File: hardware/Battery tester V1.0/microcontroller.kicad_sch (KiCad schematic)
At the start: 17 parts, among them IC4 PIC18F67J50, J1 USB_B, J2 ICP

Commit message: update man pcb, cleanup
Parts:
- removed C?: 470u/10V, Capacitor_THT:CP_Radial_D8.0mm_P3.80mm, symbol Device:C_Polarized
- removed C?: 100n, Capacitor_SMD:C_0805_2012Metric_Pad1.18x1.45mm_HandSolder, symbol Device:C
- removed LCD1: RG12864B-BIW-V, symbol My-Lib:RG12864B-BIW-V
- removed Q?: BC817, Package_TO_SOT_SMD:SOT-23, symbol Transistor_BJT:BC817
- removed R? (x2): 10k, Resistor_SMD:R_0805_2012Metric, symbol Device:R
- removed R? (x2): R, Resistor_SMD:R_1206_3216Metric, symbol Device:R
- removed R? (x2): R, Resistor_SMD:R_0805_2012Metric_Pad1.20x1.40mm_HandSolder, symbol Device:R
- removed RV?: 10k, Potentiometer_THT:Potentiometer_ACP_CA9-V10_Vertical_Hole, symbol Device:R_Potentiometer
- added C10: 1u, Capacitor_SMD:C_0805_2012Metric_Pad1.18x1.45mm_HandSolder, symbol Device:C
- added C5, C6, C7, C9: 100n, Capacitor_SMD:C_0805_2012Metric_Pad1.18x1.45mm_HandSolder, symbol Device:C
- added C8: 10u, Capacitor_SMD:C_1206_3216Metric_Pad1.33x1.80mm_HandSolder, symbol Device:C
- added J3: VCC_5V, Connector_JST:JST_XA_B02B-XASK-1_1x02_P2.50mm_Vertical, symbol Connector_Generic:Conn_01x02
- added J3, J4: LED, Connector_IDC:IDC-Header_2x05_P2.54mm_Vertical, symbol Connector_Generic:Conn_02x05_Counter_Clockwise
- added R11: 510R, symbol Device:R
- added U2: TL431DBZ, Package_TO_SOT_SMD:SOT-23, symbol Reference_Voltage:TL431DBZ
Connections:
- net +3.3V: now also C5.1, C6.1, C7.1, R11.2
- net +5V: now also J3.2 (Pin_2)
- net CS1: now also J4.6 (Pin_6)
- net CS2: now also J4.8 (Pin_8)
- net DB0: now also J4.1 (Pin_1)
- net DB1: now also J4.2 (Pin_2)
- net DB2: now also J4.3 (Pin_3)
- net DB3: now also J4.4 (Pin_4)
- net DB4: now also J4.5 (Pin_5)
- net DB5: now also J4.7 (Pin_7)
- net DB6: now also J4.9 (Pin_9)
- net DB7: now also J4.10 (Pin_10)
- net DI: now also J3.2 (Pin_2)
- net EN: now also J3.3 (Pin_3)
- net GND: now also C10.2, C5.2, C6.2, C7.2, C8.2, C9.2, J3.1 (Pin_1), U2.3 (A)
- net LCD_BACKLIGHT: now also IC4.3 (RG0/PMA8/ECCP3/P3A), J3.4 (Pin_4); no longer IC4.50 (RD6/PMD6/SCK2/SCL2)
- net ~{RST}: now also J3.1 (Pin_1); no longer IC4.51 (RD5/PMD5/SDI2/SDA2)
- net at IC4.10 (VDDCORE/VCAP): now also C8.1
- net SWITCH_RANGE: now reaches IC4.13 (RF5/AN10/C1INB/CVREF)
- net VREF_2V5: now reaches IC4.21 (RA3/AN3/VREF+)
- net VREF_2V5: now also C10.1, C9.1, R11.1, U2.1 (K), U2.2 (REF)
- net RW: no longer names the net of IC4.52 (RD4/PMD4/SDO2)
- new net COL1: J3.5 (Pin_5)
- new net COL2: J3.6 (Pin_6)
- new net COL3: J3.7 (Pin_7)
- new net ROW1: J3.8 (Pin_8)
- new net ROW2: J3.9 (Pin_9)
- new net ROW3: J3.10 (Pin_10)
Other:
- note added: "2V5 VOLTAGE REFRENCE"
- note added: "LCD, PUSH BUTTONS CONNECTORS"
- note added: "PROGRAMMING INTERFACE"
- moved on the sheet: J2, R10

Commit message: update main pcb schematic
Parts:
- added C11, C13: 100n, Capacitor_SMD:C_0805_2012Metric_Pad1.18x1.45mm_HandSolder, symbol Device:C
- added C12: 1u, Capacitor_SMD:C_0805_2012Metric_Pad1.18x1.45mm_HandSolder, symbol Device:C
- added R13, R14: 56k, Capacitor_SMD:C_0805_2012Metric_Pad1.18x1.45mm_HandSolder, symbol Device:R
- added U3: MCP4725xxx-xCH, Package_TO_SOT_SMD:SOT-23-6, symbol Analog_DAC:MCP4725xxx-xCH
- added U4: SST25VF016B, Package_SO:SOIC-8_5.3x5.3mm_P1.27mm, symbol Memory_Flash:SST25VF080B-50-4x-S2Ax
- added U5: DS18B20, Package_TO_SOT_THT:TO-92_Inline, symbol Sensor_Temperature:DS18B20
- J1: footprint (none) -> Connector_USB:USB_B_Lumberg_2411_02_Horizontal
- J5: renamed from J2; footprint (none) -> Connector_PinSocket_2.54mm:PinSocket_1x06_P2.54mm_Vertical
- R1: renamed from R11; footprint (none) -> Capacitor_SMD:C_0805_2012Metric_Pad1.18x1.45mm_HandSolder
- R2: renamed from R1; footprint (none) -> Capacitor_SMD:C_0805_2012Metric_Pad1.18x1.45mm_HandSolder
- R3: renamed from R2; footprint (none) -> Capacitor_SMD:C_0805_2012Metric_Pad1.18x1.45mm_HandSolder
- R4: renamed from R10; footprint (none) -> Capacitor_SMD:C_0805_2012Metric_Pad1.18x1.45mm_HandSolder
- renumbered C8 to C1, C6 to C2, C5 to C3, C7 to C4, C10 to C5, C9 to C6, IC4 to IC1, J3 to J2, J4 to J3, J3 to J4, U2 to U1
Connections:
- net +3.3V: now also C11.1, C12.1, C13.1, R13.2, R14.2, U3.3 (VDD), U4.3 (~{WP}), U4.7 (~{HOLD}), U4.8 (VDD), U5.3 (V_{DD})
- net DBG_UART: now also IC1.31 (RC6/TX1/CK1)
- net GND: now also C11.2, C12.2, C13.2, U3.2 (VSS), U3.6 (A0), U4.4 (VSS), U5.1 (GND)
- net PGC: now also IC1.42 (RB6/KBI2/PGC)
- net PGD: now also IC1.37 (RB7/KBI3/PGD)
- net GNDA: now reaches IC1.20 (AVSS)
- net ADC_CHARGE_VOLTAGE: now reaches IC1.22 (RA2/AN2/VREF-)
- net ADC_CHARGE_CURRENT: now reaches IC1.23 (RA1/AN1)
- net SCL: now reaches IC1.34 (RC3/SCK1/SCL1)
- net SCL: now also R13.1, U3.5 (SCL)
- net SDA: now reaches IC1.35 (RC4/SDI1/SDA1)
- net SDA: now also R14.1, U3.4 (SDA)
- net DS18B20: now reaches IC1.48 (RB0/FLT0/INT0)
- net DS18B20: now also U5.2 (DQ)
- net FLASH_CS: now reaches IC1.49 (RD7/PMD7/~{SS2})
- net FLASH_CS: now also U4.1 (~{CE})
- net FLASH_SCK: now reaches IC1.50 (RD6/PMD6/SCK2/SCL2)
- net FLASH_SCK: now also U4.6 (SCK)
- net FLASH_SDI: now reaches IC1.51 (RD5/PMD5/SDI2/SDA2)
- net FLASH_SDI: now also U4.5 (SI)
- net FLASH_SDO: now reaches IC1.52 (RD4/PMD4/SDO2)
- net FLASH_SDO: now also U4.2 (SO)
- new net DAC_CURRENT: U3.1 (VOUT)
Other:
- note added: "12BIT I2C DAC FOR CURRENT REGULATION"
- note added: "16MBIT SPI FLASH MEMORY"

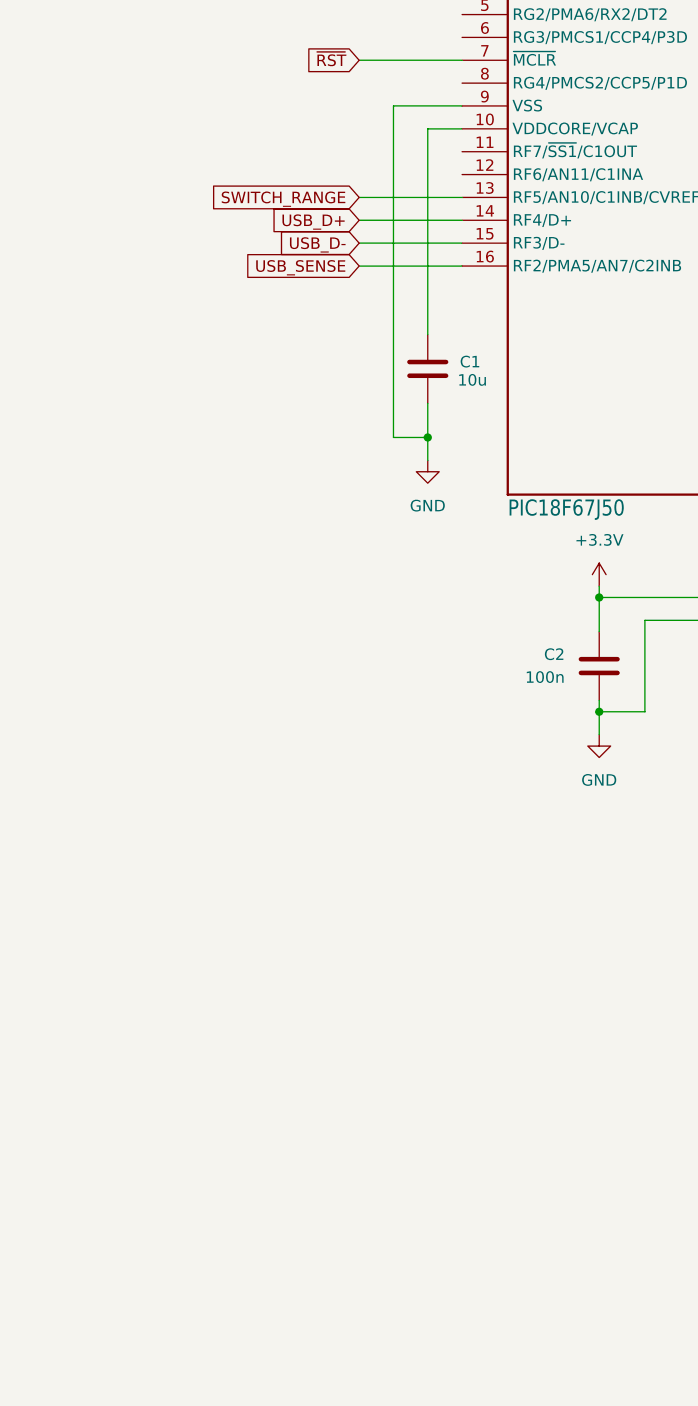
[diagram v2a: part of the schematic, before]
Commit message: update main pcb battery charger
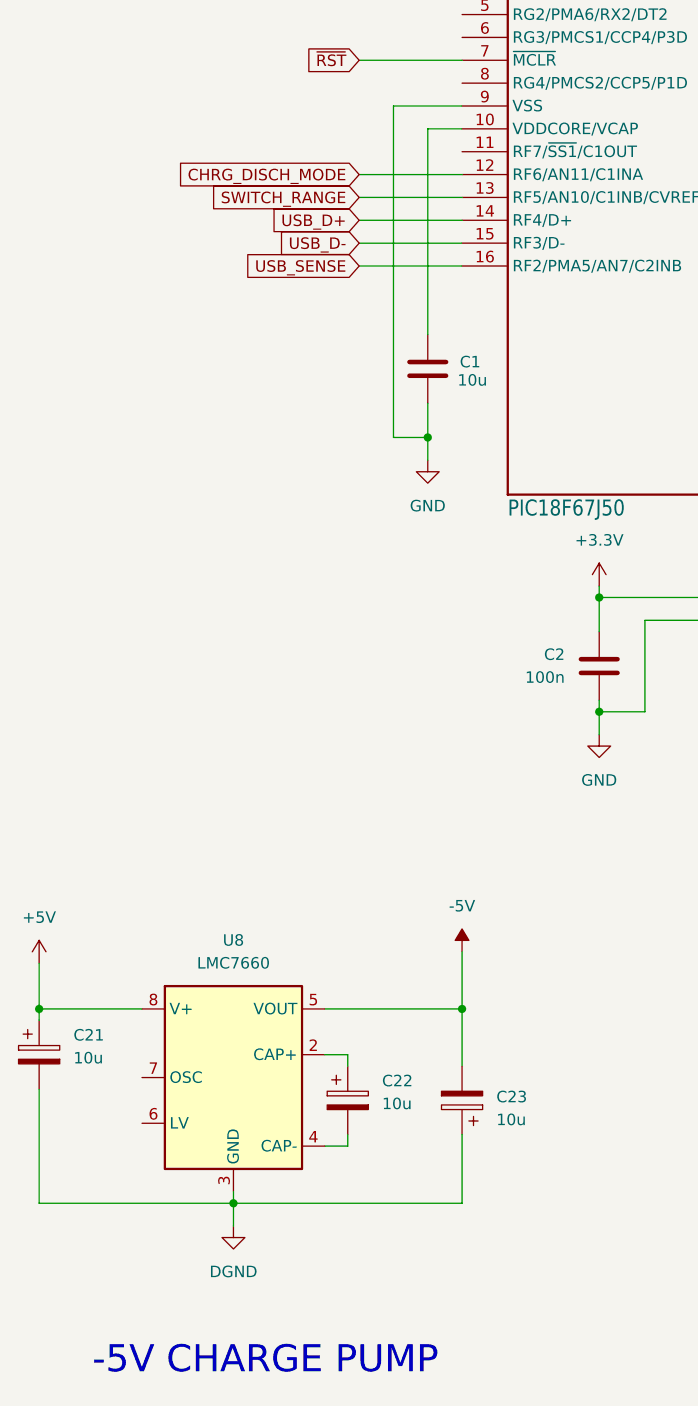
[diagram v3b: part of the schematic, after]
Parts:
- added C21, C22, C23: 10u, Capacitor_Tantalum_SMD:CP_EIA-3528-12_Kemet-T, symbol Device:C_Polarized
- added U8: LMC7660, Package_SO:SOIC-8_3.9x4.9mm_P1.27mm, symbol Regulator_SwitchedCapacitor:LMC7660
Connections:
- net +5V: now also C21.1, U8.8 (V+)
- net CHRG_DISCH_MODE: now reaches IC1.12 (RF6/AN11/C1INA)
- new net: C22.1, U8.2 (CAP+)
- new net: C22.2, U8.4 (CAP-)
- new net -5V: C23.2, U8.5 (VOUT)
- new net DGND: C21.2, C23.1, U8.3 (GND)
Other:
- note added: "-5V CHARGE PUMP"

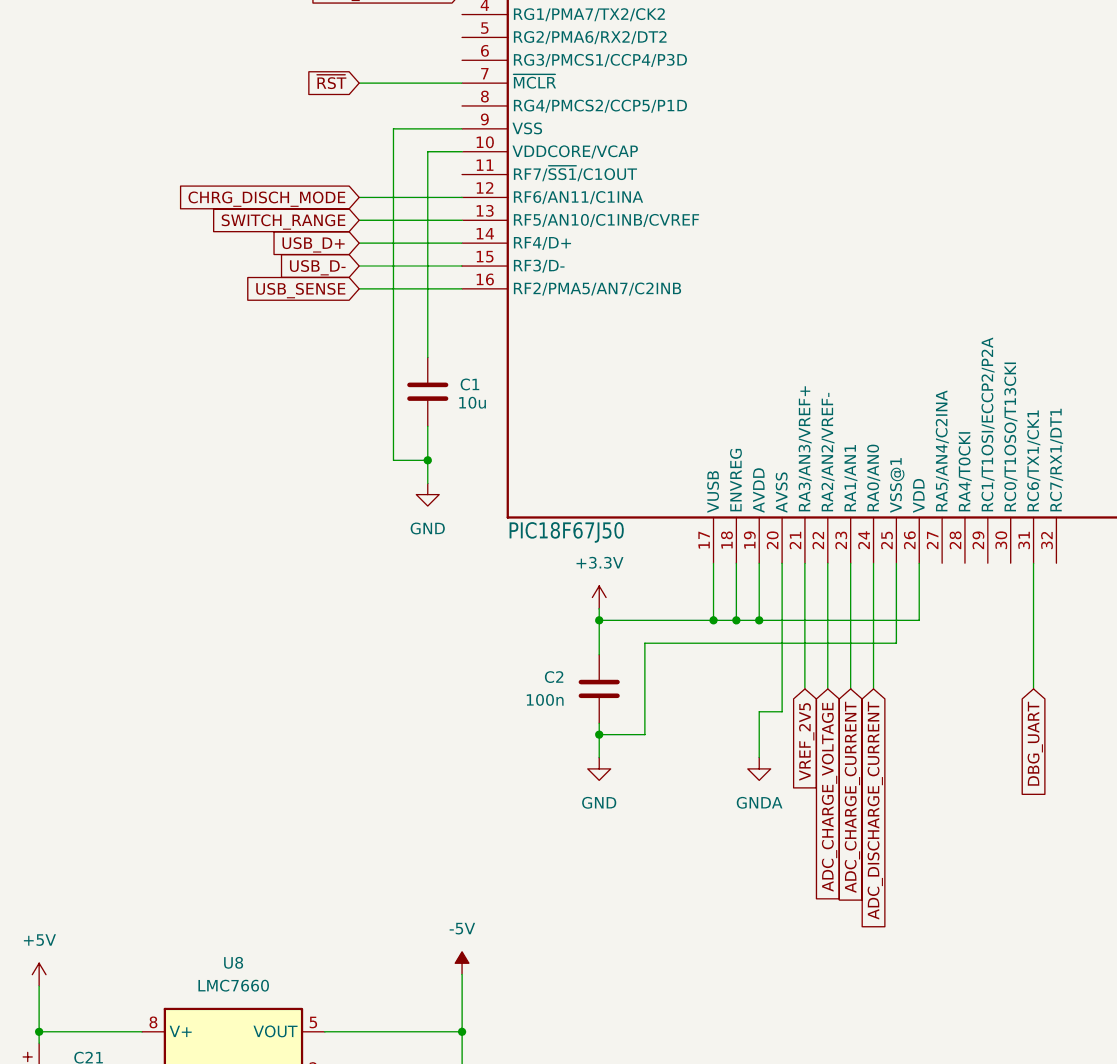
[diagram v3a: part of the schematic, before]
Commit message: update charger schematic - voltage measurement
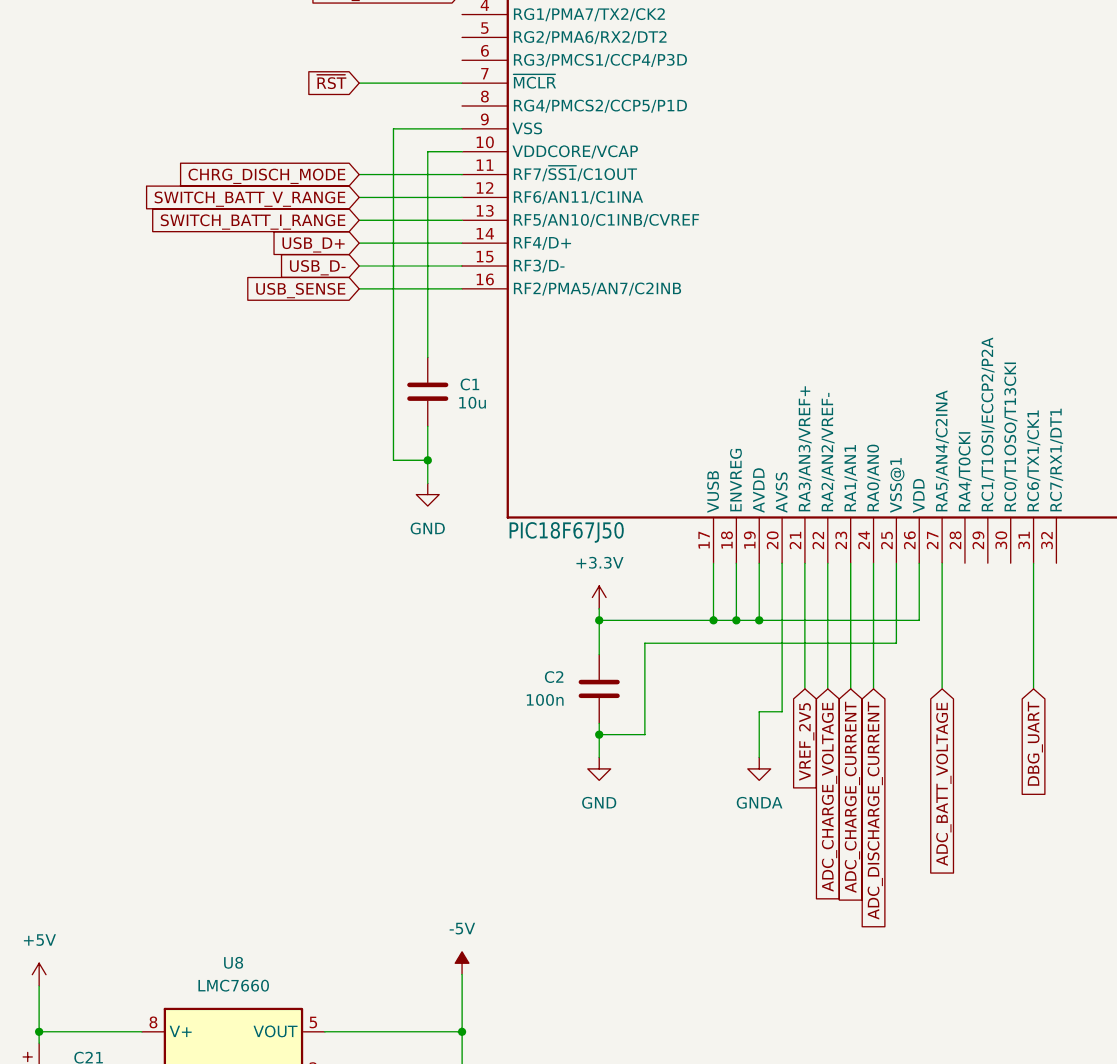
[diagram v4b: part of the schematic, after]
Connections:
- net CHRG_DISCH_MODE: now also IC1.11 (RF7/~{SS1}/C1OUT); no longer IC1.12 (RF6/AN11/C1INA)
- net ADC_BATT_VOLTAGE: now reaches IC1.27 (RA5/AN4/C2INA)
- net SWITCH_RANGE renamed SWITCH_BATT_I_RANGE
- new net SWITCH_BATT_V_RANGE: IC1.12 (RF6/AN11/C1INA)

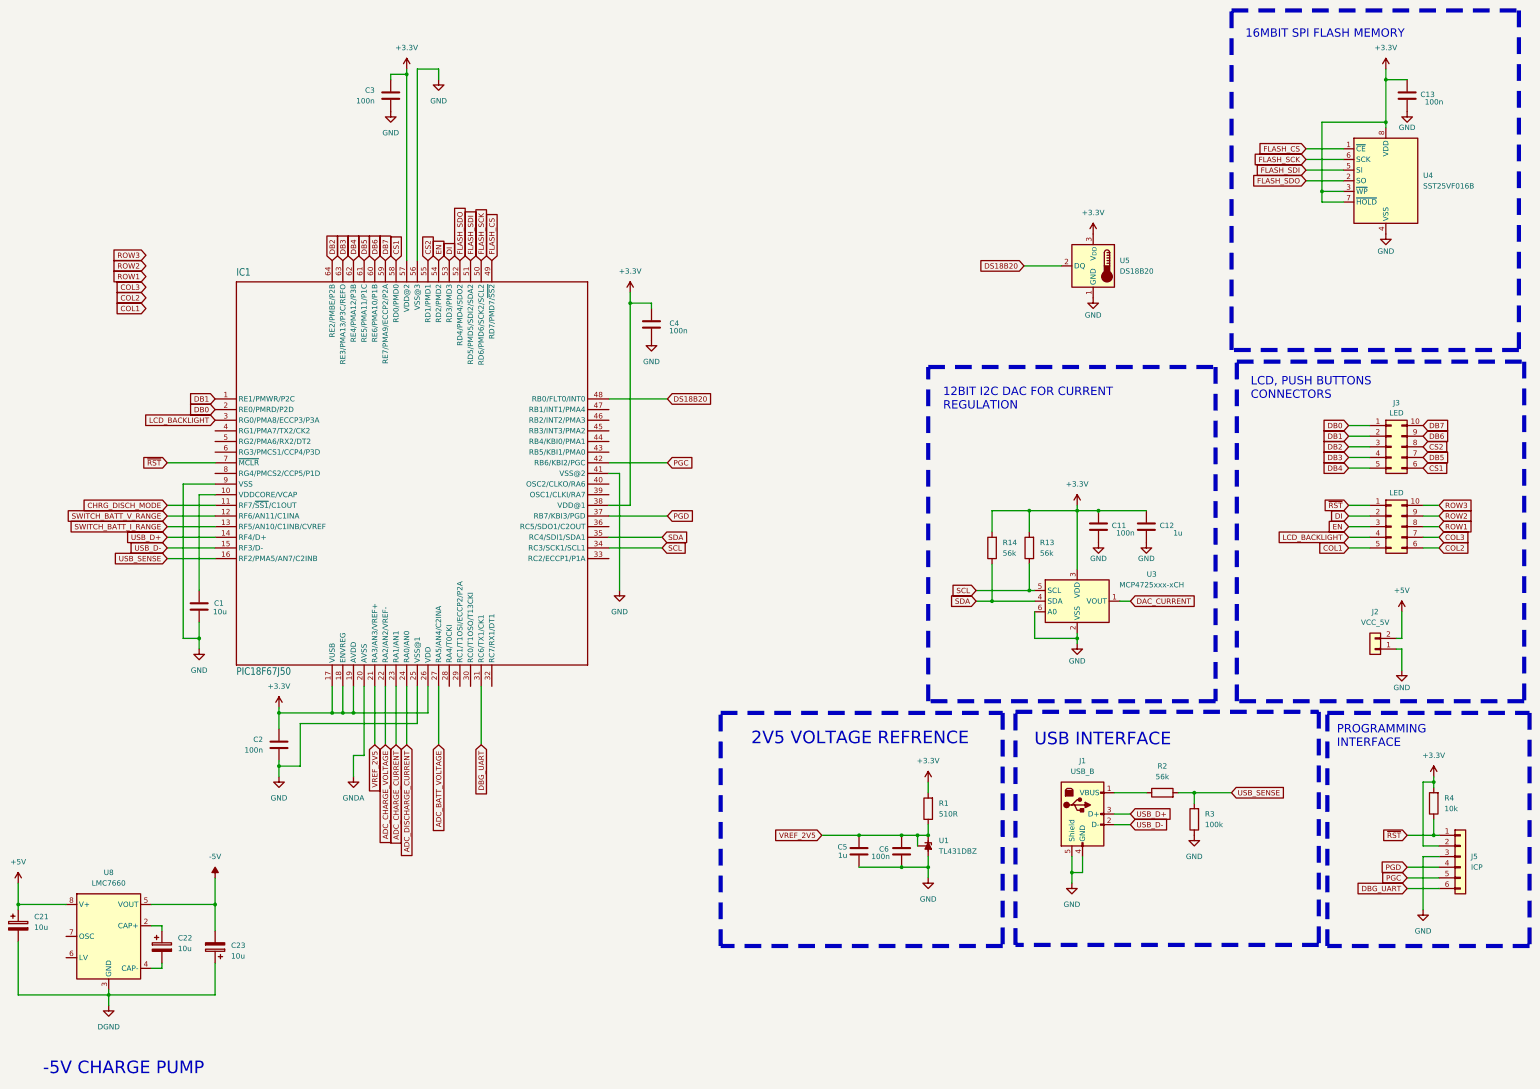
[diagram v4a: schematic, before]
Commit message: update schematic
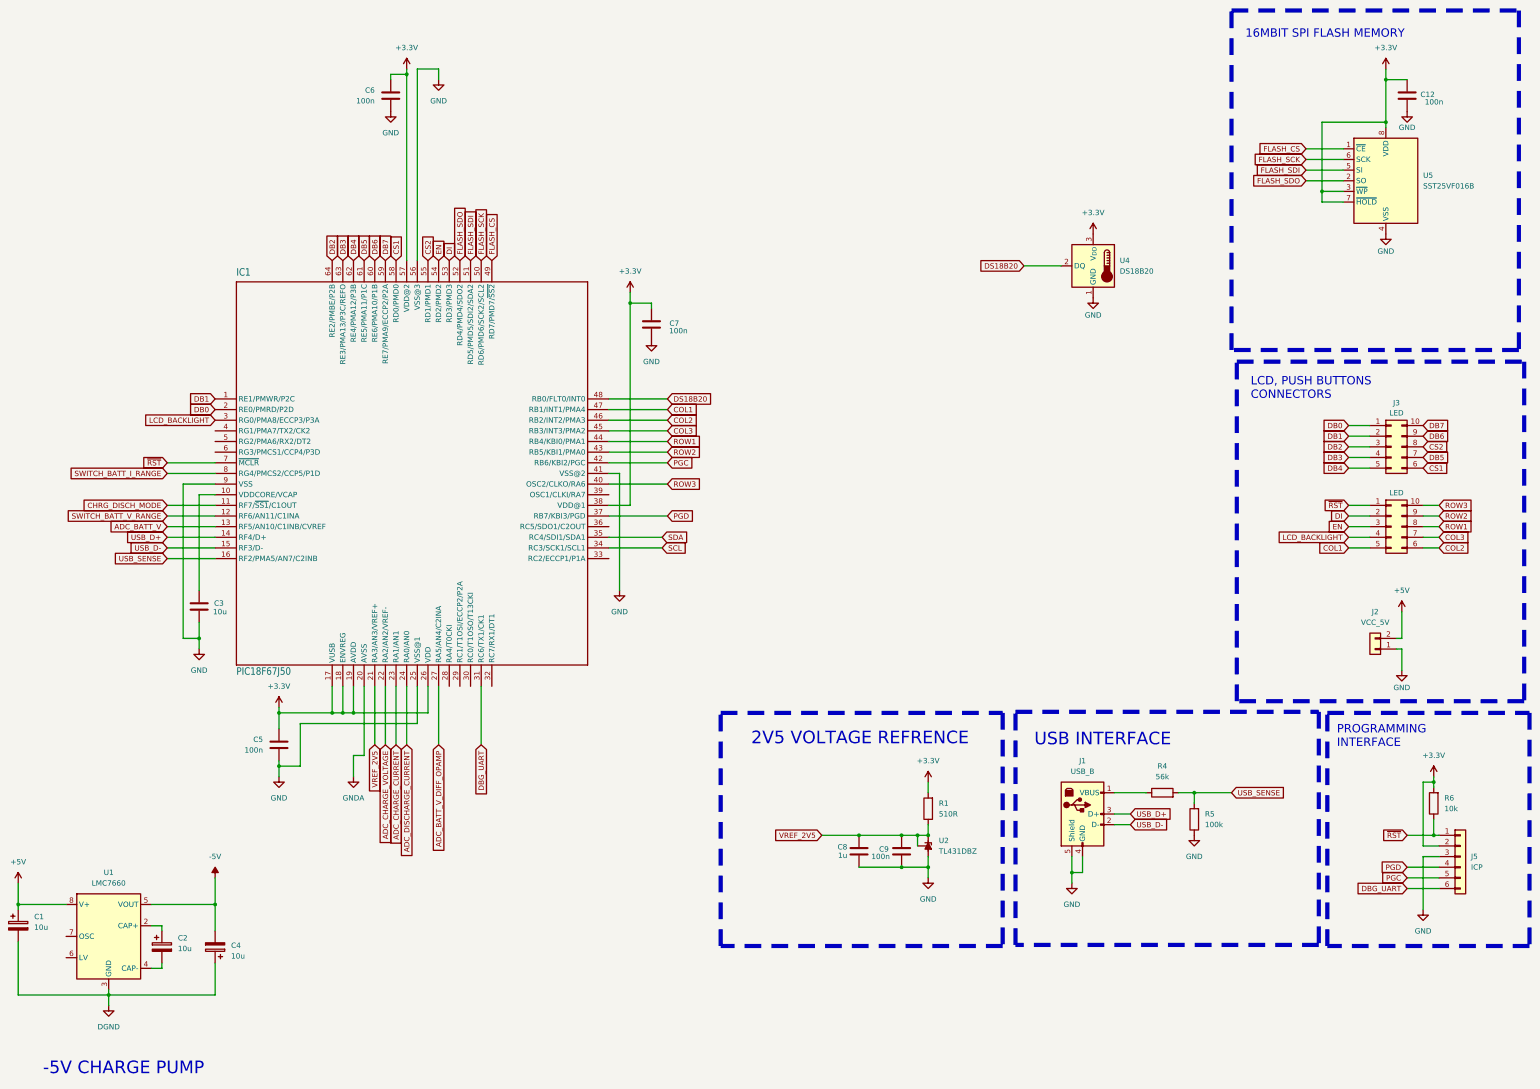
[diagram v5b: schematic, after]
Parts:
- removed C11: 100n, Capacitor_SMD:C_0805_2012Metric_Pad1.18x1.45mm_HandSolder, symbol Device:C
- removed C12: 1u, Capacitor_SMD:C_0805_2012Metric_Pad1.18x1.45mm_HandSolder, symbol Device:C
- removed R13, R14: 56k, Capacitor_SMD:C_0805_2012Metric_Pad1.18x1.45mm_HandSolder, symbol Device:R
- removed U3: MCP4725xxx-xCH, Package_TO_SOT_SMD:SOT-23-6, symbol Analog_DAC:MCP4725xxx-xCH
- renumbered C21 to C1, C13 to C12, C22 to C2, C1 to C3, C23 to C4, C2 to C5, C3 to C6, C4 to C7, C5 to C8, C6 to C9, R2 to R4, R3 to R5, R4 to R6, U8 to U1, U1 to U2, U5 to U4, U4 to U5
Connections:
- net COL1: now also IC1.47 (RB1/INT1/PMA4)
- net COL2: now also IC1.46 (RB2/INT2/PMA3)
- net COL3: now also IC1.45 (RB3/INT3/PMA2)
- net ROW1: now also IC1.44 (RB4/KBI0/PMA1)
- net ROW2: now also IC1.43 (RB5/KBI1/PMA0)
- net ROW3: now also IC1.40 (OSC2/CLKO/RA6)
- net SWITCH_BATT_I_RANGE: now also IC1.8 (RG4/PMCS2/CCP5/P1D); no longer IC1.13 (RF5/AN10/C1INB/CVREF)
- net ADC_BATT_VOLTAGE renamed ADC_BATT_V_DIFF_OPAMP
- new net ADC_BATT_V: IC1.13 (RF5/AN10/C1INB/CVREF)
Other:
- note removed: "12BIT I2C DAC FOR CURRENT REGULATION"
